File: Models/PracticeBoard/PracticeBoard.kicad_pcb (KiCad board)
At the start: 2 copper layers, 0 parts

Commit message: Rough sketch of the layout resulted in a calculated price of
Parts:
- added J1: Conn_01x02_Pin, Connector_Custom:PinHeader_1x2, F.Cu at (154.2, 99.0)
- added R1: 10k, 0603, TwoTerminal:RESC0603, F.Cu at (126.4, 99.6)
- added R10: 10k, 0603, TwoTerminal:RESC0603, F.Cu at (144.4, 99.6)
- added R11: 10k, 0603, TwoTerminal:RESC0603, F.Cu at (144.3, 101.5)
- added R12: 10k, 0603, TwoTerminal:RESC0603, F.Cu at (144.3, 103.3)
- added R13: 10k, 0603, TwoTerminal:RESC0603, F.Cu at (144.3, 105.0)
- added R14: 10k, 0603, TwoTerminal:RESC0603, F.Cu at (144.3, 106.8)
- added R15: 10k, 0603, TwoTerminal:RESC0603, F.Cu at (144.3, 108.6)
- added R16: 10k, 0603, TwoTerminal:RESC0603, F.Cu at (144.3, 110.4)
- added R17: 10k, 0603, TwoTerminal:RESC0603, F.Cu at (144.3, 112.1)
- added R2: 10k, 0805, TwoTerminal:RESC0805, F.Cu at (149.3, 100.3)
- added R3: 10k, 0603, TwoTerminal:RESC0603, F.Cu at (126.3, 101.4)
- added R4: 10k, 0603, TwoTerminal:RESC0603, F.Cu at (126.3, 103.2)
- added R5: 10k, 0603, TwoTerminal:RESC0603, F.Cu at (126.4, 105.1)
- added R6: 10k, 0603, TwoTerminal:RESC0603, F.Cu at (126.4, 106.8)
- added R7: 10k, 0603, TwoTerminal:RESC0603, F.Cu at (126.4, 108.6)
- added R8: 10k, 0603, TwoTerminal:RESC0603, F.Cu at (126.4, 110.4)
- added R9: 10k, 0603, TwoTerminal:RESC0603, F.Cu at (126.4, 112.2)
- added U1: XMC1100, IC:ADS8699, F.Cu at (135.4, 106.0)
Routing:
- net Net-(U1-DGND): track 0.00 -> 6.88 mm
- net Net-(U1-AIN_GND): track 0.00 -> 6.86 mm
- net Net-(U1-DVDD): track 0.00 -> 6.84 mm
- net Net-(U1-*RST): track 0.00 -> 6.66 mm
- net Net-(U1-AVDD): track 0.00 -> 6.45 mm
- net Net-(U1-AIN_P): track 0.00 -> 6.33 mm
- net Net-(U1-RVS): track 0.00 -> 6.31 mm
- net Net-(U1-SDI): track 0.00 -> 6.20 mm
- net Net-(U1-AGND): track 0.00 -> 5.96 mm
- net Net-(U1-REFCAP): track 0.00 -> 5.86 mm
- net Net-(U1-ALARM/SDO-1/GPO): track 0.00 -> 5.84 mm
- net Net-(U1-CONVST/*CS): track 0.00 -> 5.78 mm
- net Net-(U1-REFGND): track 0.00 -> 5.43 mm
- net Net-(U1-REFIO): track 0.00 -> 5.41 mm
- net Net-(U1-SDO-0): track 0.00 -> 5.33 mm
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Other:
- board text added: "Rough sketch of what the layout will look like. In the final draft, it will obviously have more rule-based spacing and alignment between parts."

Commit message: Finally settled on the relative layout of all parts on the board
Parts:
- moved J1 3.28 mm to (153.7, 102.2)
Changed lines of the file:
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@@
 	(footprint "Connector_Custom:PinHeader_1x2"
 		(layer "F.Cu")
-		(at 154.2 99.01)
+		(at 153.72 102.25)
 		(property "Reference" "J1"
 			(at 0.0025 -3.5625 0)
 			(unlocked yes)
 			(layer "F.SilkS")
+			(hide yes)
 			(effects
 				(font
@@
 		(layer "Cmts.User")
 		(pts
-			(xy 123.96 96.81) (xy 147.06 97.75)
+			(xy 123.96 96.81) (xy 156.08 97.59)
 		)
 		(height -2.32)
@@
 			(keep_text_aligned yes)
 		)
-		(gr_text "23.1"
-			(at 135.51 93.57 0)
+		(gr_text "32.12"
+			(at 140.02 93.57 0)
 			(layer "Cmts.User")
 			(effects

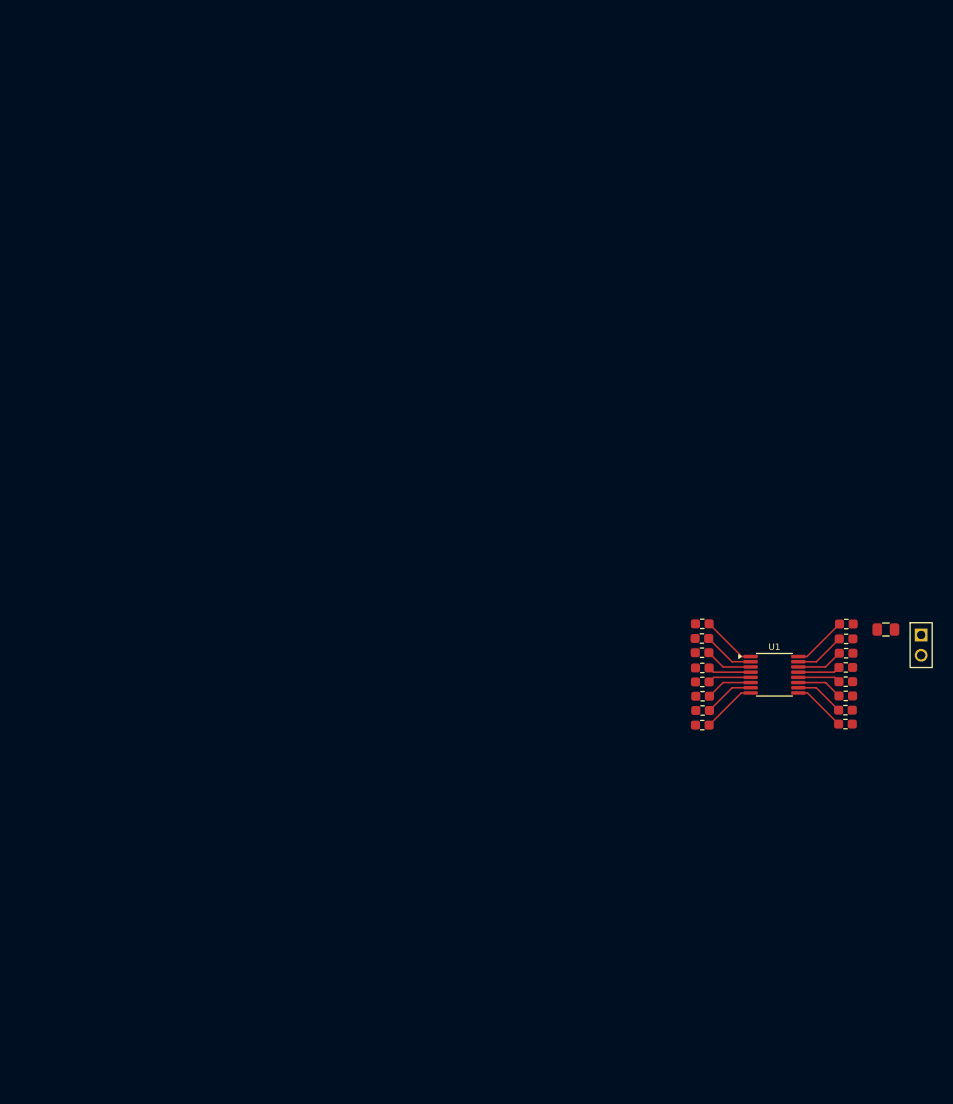
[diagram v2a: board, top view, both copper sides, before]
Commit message: Aligned the U1 and U2 subsystems
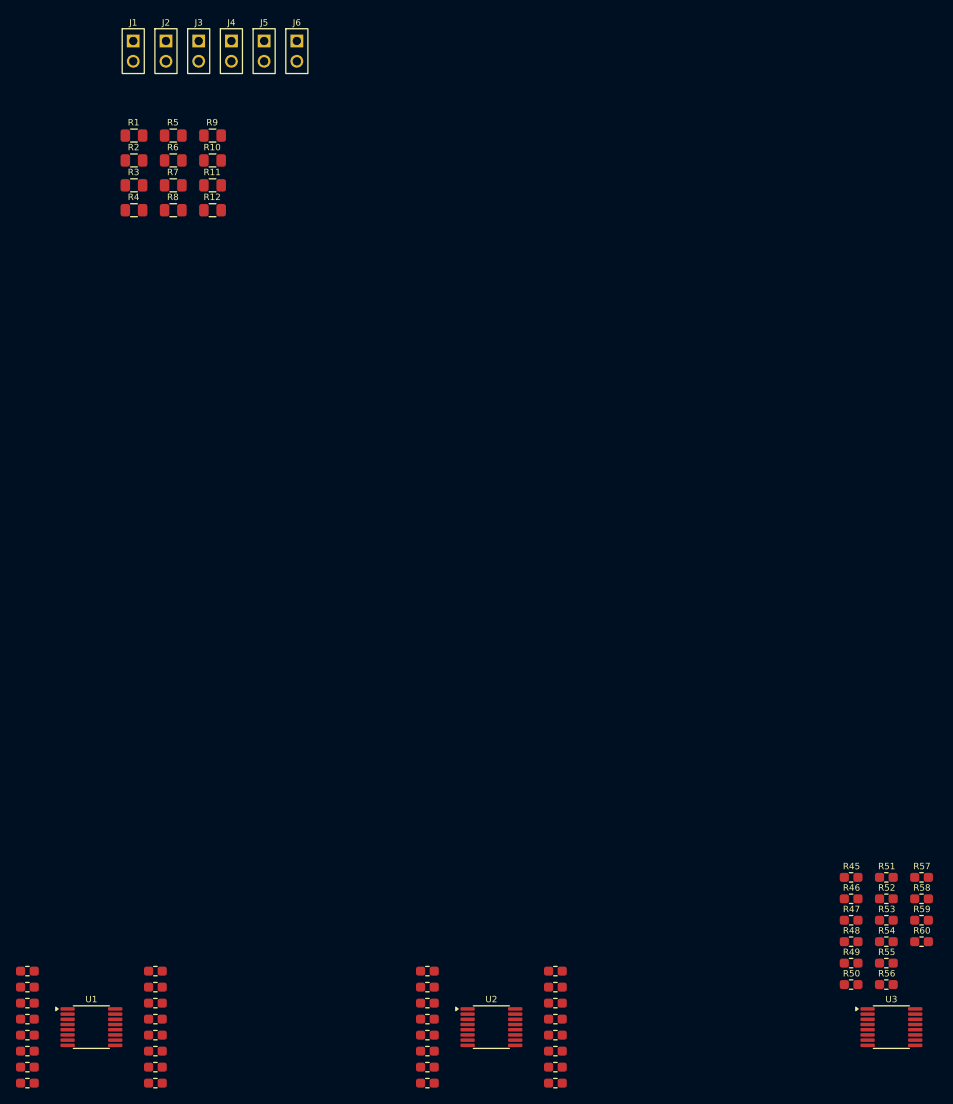
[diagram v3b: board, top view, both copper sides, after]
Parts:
- added J2: Conn_01x02_Pin, Connector_Custom:PinHeader_1x2, F.Cu at (59.3, 28.0)
- added J3: Conn_01x02_Pin, Connector_Custom:PinHeader_1x2, F.Cu at (63.4, 28.0)
- added J4: Conn_01x02_Pin, Connector_Custom:PinHeader_1x2, F.Cu at (67.5, 28.0)
- added J5: Conn_01x02_Pin, Connector_Custom:PinHeader_1x2, F.Cu at (71.6, 28.0)
- added J6: Conn_01x02_Pin, Connector_Custom:PinHeader_1x2, F.Cu at (75.7, 28.0)
- added R18: 10k, 0603, TwoTerminal:RESC0603, F.Cu at (42.0, 155.0)
- added R19: 10k, 0603, TwoTerminal:RESC0603, F.Cu at (42.0, 143.0)
- added R20: 10k, 0603, TwoTerminal:RESC0603, F.Cu at (42.0, 157.0)
- added R21: 10k, 0603, TwoTerminal:RESC0603, F.Cu at (58.0, 143.0)
- added R22: 10k, 0603, TwoTerminal:RESC0603, F.Cu at (58.0, 157.0)
- added R23: 10k, 0603, TwoTerminal:RESC0603, F.Cu at (58.0, 145.0)
- added R24: 10k, 0603, TwoTerminal:RESC0603, F.Cu at (58.0, 155.0)
- added R25: 10k, 0603, TwoTerminal:RESC0603, F.Cu at (58.0, 147.0)
- added R26: 10k, 0603, TwoTerminal:RESC0603, F.Cu at (58.0, 153.0)
- added R27: 10k, 0603, TwoTerminal:RESC0603, F.Cu at (58.0, 149.0)
- added R28: 10k, 0603, TwoTerminal:RESC0603, F.Cu at (58.0, 151.0)
- added R29: 10k, 0603, TwoTerminal:RESC0603, F.Cu at (92.0, 149.0)
- added R30: 10k, 0603, TwoTerminal:RESC0603, F.Cu at (92.0, 151.0)
- added R31: 10k, 0603, TwoTerminal:RESC0603, F.Cu at (92.0, 147.0)
- added R32: 10k, 0603, TwoTerminal:RESC0603, F.Cu at (92.0, 153.0)
- added R33: 10k, 0603, TwoTerminal:RESC0603, F.Cu at (92.0, 145.0)
- added R34: 10k, 0603, TwoTerminal:RESC0603, F.Cu at (92.0, 155.0)
- added R35: 10k, 0603, TwoTerminal:RESC0603, F.Cu at (92.0, 143.0)
- added R36: 10k, 0603, TwoTerminal:RESC0603, F.Cu at (92.0, 157.0)
- added R37: 10k, 0603, TwoTerminal:RESC0603, F.Cu at (108.0, 143.0)
- added R38: 10k, 0603, TwoTerminal:RESC0603, F.Cu at (108.0, 157.0)
- added R39: 10k, 0603, TwoTerminal:RESC0603, F.Cu at (108.0, 145.0)
- added R40: 10k, 0603, TwoTerminal:RESC0603, F.Cu at (108.0, 155.0)
- added R41: 10k, 0603, TwoTerminal:RESC0603, F.Cu at (108.0, 147.0)
- added R42: 10k, 0603, TwoTerminal:RESC0603, F.Cu at (108.0, 153.0)
- added R43: 10k, 0603, TwoTerminal:RESC0603, F.Cu at (108.0, 149.0)
- added R44: 10k, 0603, TwoTerminal:RESC0603, F.Cu at (108.0, 151.0)
- added R45: 10k, 0603, TwoTerminal:RESC0603, F.Cu at (145.0, 131.3)
- added R46: 10k, 0603, TwoTerminal:RESC0603, F.Cu at (145.0, 134.0)
- added R47: 10k, 0603, TwoTerminal:RESC0603, F.Cu at (145.0, 136.6)
- added R48: 10k, 0603, TwoTerminal:RESC0603, F.Cu at (145.0, 139.3)
- added R49: 10k, 0603, TwoTerminal:RESC0603, F.Cu at (145.0, 142.0)
- added R50: 10k, 0603, TwoTerminal:RESC0603, F.Cu at (145.0, 144.7)
- added R51: 10k, 0603, TwoTerminal:RESC0603, F.Cu at (149.4, 131.3)
- added R52: 10k, 0603, TwoTerminal:RESC0603, F.Cu at (149.4, 134.0)
- added R53: 10k, 0603, TwoTerminal:RESC0603, F.Cu at (149.4, 136.6)
- added R54: 10k, 0603, TwoTerminal:RESC0603, F.Cu at (149.4, 139.3)
- added R55: 10k, 0603, TwoTerminal:RESC0603, F.Cu at (149.4, 142.0)
- added R56: 10k, 0603, TwoTerminal:RESC0603, F.Cu at (149.4, 144.7)
- added R57: 10k, 0603, TwoTerminal:RESC0603, F.Cu at (153.8, 131.3)
- added R58: 10k, 0603, TwoTerminal:RESC0603, F.Cu at (153.8, 134.0)
- added R59: 10k, 0603, TwoTerminal:RESC0603, F.Cu at (153.8, 136.6)
- added R60: 10k, 0603, TwoTerminal:RESC0603, F.Cu at (153.8, 139.3)
- added U2: XMC1100, IC:ADS8699, F.Cu at (100.0, 150.0)
- added U3: XMC1100, IC:ADS8699, F.Cu at (150.0, 150.0)
- R1, R10, R11, R12, R3, R4, R5, R6, R7, R8, R9: value 10k, 0603 -> 10k, 0805; footprint TwoTerminal:RESC0603 -> TwoTerminal:RESC0805
- moved J1 123.3 mm to (55.2, 28.0)
- moved R14 111.4 mm to (42.0, 151.0)
- moved R13 111.3 mm to (42.0, 149.0)
- moved R16 110.8 mm to (42.0, 153.0)
- moved R2 110.8 mm to (55.3, 41.7)
- moved R15 109.3 mm to (42.0, 147.0)
- moved R17 107.4 mm to (42.0, 145.0)
- moved R10 98.2 mm to (65.1, 41.7)
- moved R11 97.4 mm to (65.1, 44.8)
- moved R12 96.6 mm to (65.1, 47.9)
- moved U1 96.1 mm to (50.0, 150.0)
- moved R9 95.8 mm to (65.1, 38.6)
- moved R5 93.8 mm to (60.2, 38.6)
- moved R1 93.7 mm to (55.3, 38.6)
- moved R6 92.9 mm to (60.2, 41.7)
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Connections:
- R1 pad 2: Net-(U1-DGND) -> unconnected-(R1-Pad2)
- R10 pad 1: Net-(U1-DVDD) -> unconnected-(R10-Pad1)
- R11 pad 1: Net-(U1-RVS) -> unconnected-(R11-Pad1)
- R12 pad 1: Net-(U1-ALARM/SDO-1/GPO) -> unconnected-(R12-Pad1)
- R13 pad 1: Net-(U1-SDO-0) -> unconnected-(R13-Pad1)
- R13 pad 2: unconnected-(R13-Pad2) -> Net-(U1-REFIO)
- R14 pad 1: Net-(U1-SCLK) -> unconnected-(R14-Pad1)
- R14 pad 2: unconnected-(R14-Pad2) -> Net-(U1-REFGND)
- R15 pad 1: Net-(U1-CONVST/*CS) -> unconnected-(R15-Pad1)
- R15 pad 2: unconnected-(R15-Pad2) -> Net-(U1-AGND)
- R16 pad 1: Net-(U1-SDI) -> unconnected-(R16-Pad1)
- R16 pad 2: unconnected-(R16-Pad2) -> Net-(U1-REFCAP)
- R17 pad 1: Net-(U1-*RST) -> unconnected-(R17-Pad1)
- R17 pad 2: unconnected-(R17-Pad2) -> Net-(U1-AVDD)
- R3 pad 2: Net-(U1-AVDD) -> unconnected-(R3-Pad2)
- R4 pad 2: Net-(U1-AGND) -> unconnected-(R4-Pad2)
- R5 pad 2: Net-(U1-REFIO) -> unconnected-(R5-Pad2)
- R6 pad 2: Net-(U1-REFGND) -> unconnected-(R6-Pad2)
- R7 pad 2: Net-(U1-REFCAP) -> unconnected-(R7-Pad2)
- R8 pad 2: Net-(U1-AIN_P) -> unconnected-(R8-Pad2)
- R9 pad 2: Net-(U1-AIN_GND) -> unconnected-(R9-Pad2)
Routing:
- net Net-(U1-DGND): track 6.88 -> 0.00 mm
- net Net-(U1-AIN_GND): track 6.86 -> 0.00 mm
- net Net-(U1-DVDD): track 6.84 -> 0.00 mm
- net Net-(U1-*RST): track 6.66 -> 0.00 mm
- net Net-(U1-AVDD): track 6.45 -> 0.00 mm
- net Net-(U1-AIN_P): track 6.33 -> 0.00 mm
- net Net-(U1-RVS): track 6.31 -> 0.00 mm
- net Net-(U1-SDI): track 6.20 -> 0.00 mm
- net Net-(U1-AGND): track 5.96 -> 0.00 mm
- net Net-(U1-REFCAP): track 5.86 -> 0.00 mm
- net Net-(U1-ALARM/SDO-1/GPO): track 5.84 -> 0.00 mm
- net Net-(U1-CONVST/*CS): track 5.78 -> 0.00 mm
- net Net-(U1-REFGND): track 5.43 -> 0.00 mm
- net Net-(U1-REFIO): track 5.41 -> 0.00 mm
- net Net-(U1-SDO-0): track 5.33 -> 0.00 mm
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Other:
- board text removed: "Rough sketch of what the layout will look like. In the final draft, it will obviously have more rule-based spacing and alignment between parts."

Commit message: Fixed some of the silkscreen for the battery module
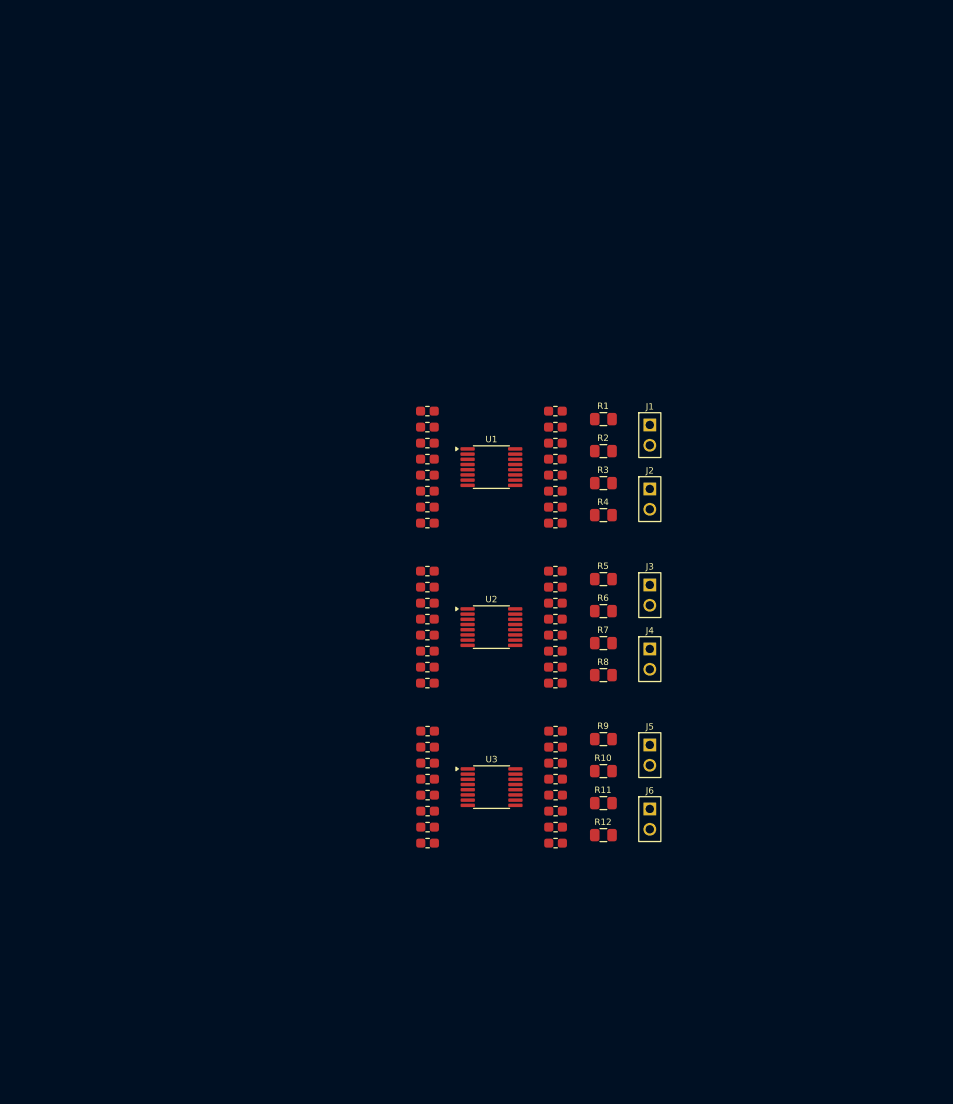
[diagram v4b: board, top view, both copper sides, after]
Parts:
- moved J6 105.7 mm to (119.8, 124.0)
- moved J5 100.3 mm to (119.8, 116.0)
- moved J4 92.3 mm to (119.8, 104.0)
- moved R12 92.1 mm to (114.0, 126.0)
- moved R11 91.4 mm to (114.0, 122.0)
- moved R10 90.6 mm to (114.0, 118.0)
- moved R9 89.9 mm to (114.0, 114.0)
- moved J3 88.3 mm to (119.8, 96.0)
- moved R13 86.0 mm to (92.0, 79.0)
- moved R14 86.0 mm to (92.0, 81.0)
- moved R15 86.0 mm to (92.0, 77.0)
- moved R16 86.0 mm to (92.0, 83.0)
- moved R17 86.0 mm to (92.0, 75.0)
- moved R18 86.0 mm to (92.0, 85.0)
- moved R19 86.0 mm to (92.0, 73.0)
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
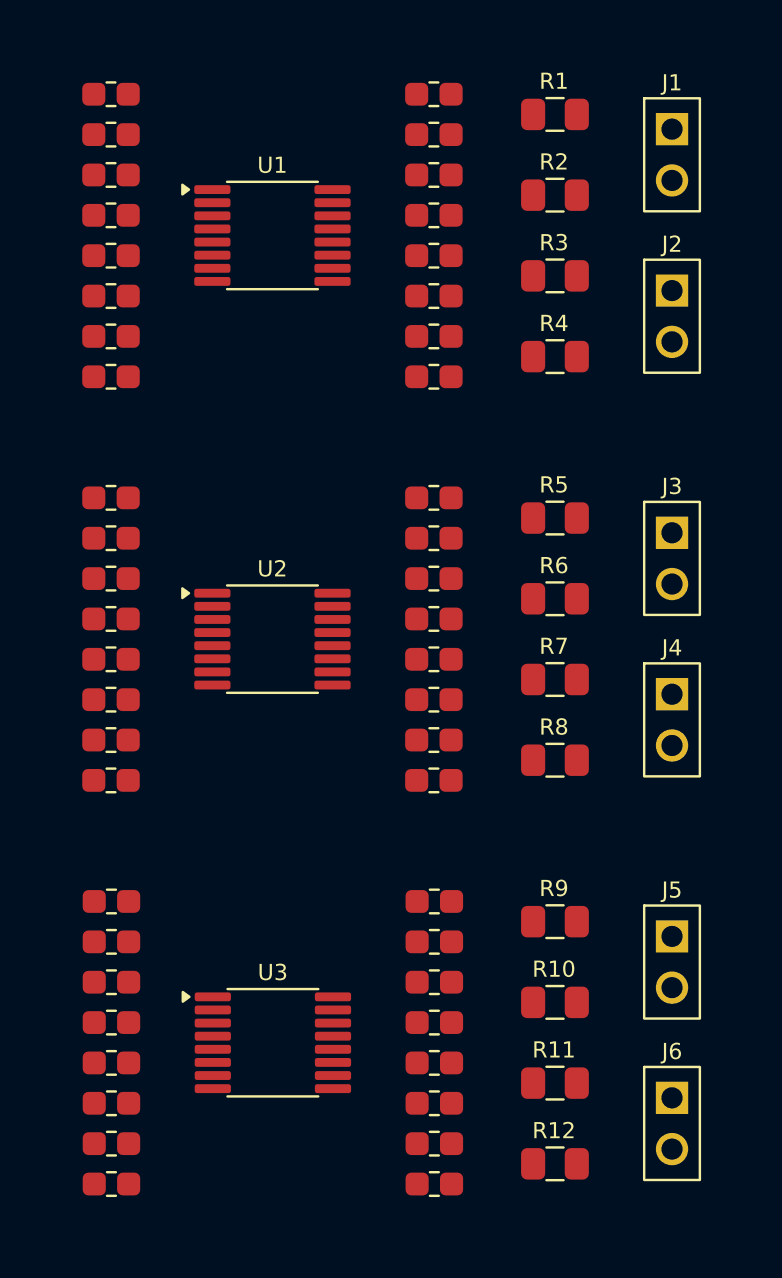
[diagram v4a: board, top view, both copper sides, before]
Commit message: Wired everything up, but next step is to connect half of the THT and 0805 to a ground plane
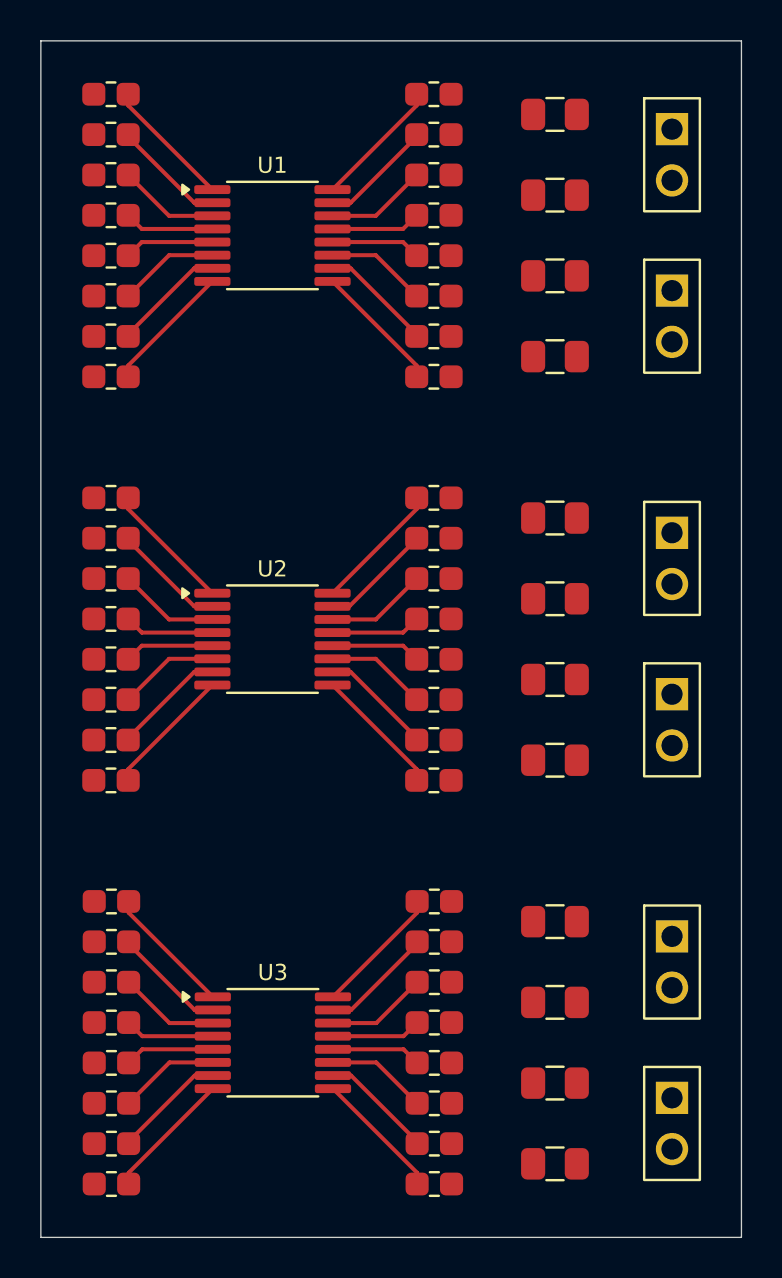
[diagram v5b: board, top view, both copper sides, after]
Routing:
- net Net-(U3-DVDD): track 0.00 -> 6.45 mm
- net Net-(U3-DGND): track 0.00 -> 6.45 mm
- net Net-(U3-AIN_GND): track 0.00 -> 6.45 mm
- net Net-(U3-*RST): track 0.00 -> 6.45 mm
- net Net-(U2-DVDD): track 0.00 -> 6.45 mm
- net Net-(U2-DGND): track 0.00 -> 6.45 mm
- net Net-(U2-AIN_GND): track 0.00 -> 6.45 mm
- net Net-(U2-*RST): track 0.00 -> 6.45 mm
- net Net-(U1-DVDD): track 0.00 -> 6.45 mm
- net Net-(U1-DGND): track 0.00 -> 6.45 mm
- net Net-(U1-AIN_GND): track 0.00 -> 6.45 mm
- net Net-(U1-*RST): track 0.00 -> 6.45 mm
- net Net-(U3-AVDD): track 0.00 -> 5.63 mm
- net Net-(U3-AIN_P): track 0.00 -> 5.63 mm
- net Net-(U3-SDI): track 0.00 -> 5.63 mm
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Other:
- board outline added: 34.7 x 59.3 mm

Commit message: Finished the layout of the practice board
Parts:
- R10, R11, R12, R7, R8, R9: moved to B.Cu
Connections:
- J4 pad 1: unconnected-(J4-Pin_1-Pad1) -> GND
- J4 pad 2: unconnected-(J4-Pin_2-Pad2) -> GND
- J5 pad 1: unconnected-(J5-Pin_1-Pad1) -> GND
- J5 pad 2: unconnected-(J5-Pin_2-Pad2) -> GND
- J6 pad 1: unconnected-(J6-Pin_1-Pad1) -> GND
- J6 pad 2: unconnected-(J6-Pin_2-Pad2) -> GND
- R10 pad 1: unconnected-(R10-Pad1) -> GND
- R10 pad 2: unconnected-(R10-Pad2) -> GND
- R11 pad 1: unconnected-(R11-Pad1) -> GND
- R11 pad 2: unconnected-(R11-Pad2) -> GND
- R12 pad 1: unconnected-(R12-Pad1) -> GND
- R12 pad 2: unconnected-(R12-Pad2) -> GND
- R7 pad 1: unconnected-(R7-Pad1) -> GND
- R7 pad 2: unconnected-(R7-Pad2) -> GND
- R8 pad 1: unconnected-(R8-Pad1) -> GND
- R8 pad 2: unconnected-(R8-Pad2) -> GND
- R9 pad 1: unconnected-(R9-Pad1) -> GND
- R9 pad 2: unconnected-(R9-Pad2) -> GND
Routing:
- added copper zone on B.Cu, net GND
